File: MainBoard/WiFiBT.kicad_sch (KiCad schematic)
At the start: 8 parts, among them U2 ESP32-MINI-1-H4

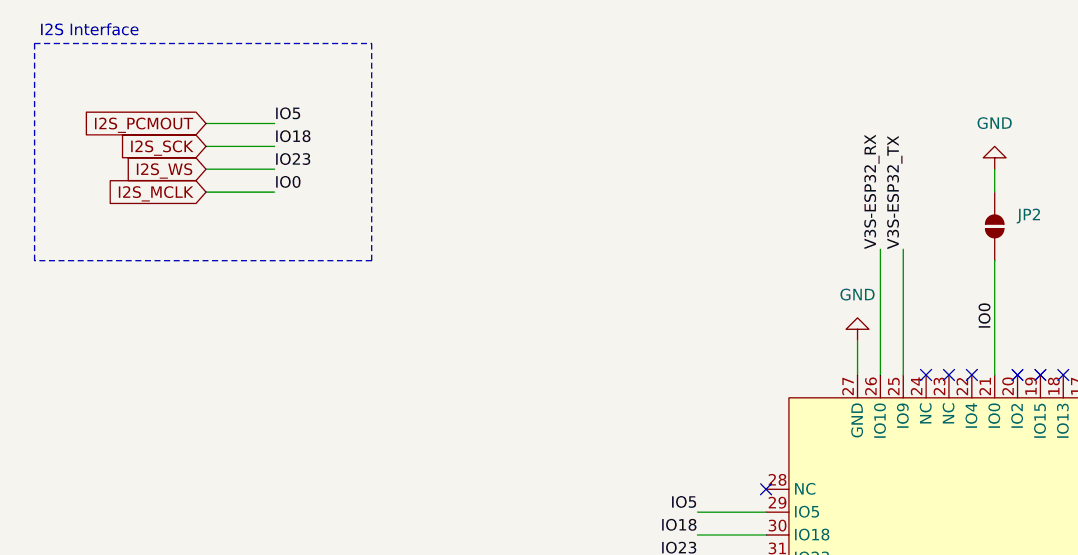
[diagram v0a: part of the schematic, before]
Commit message: footprints for wheel + power changes for v3s
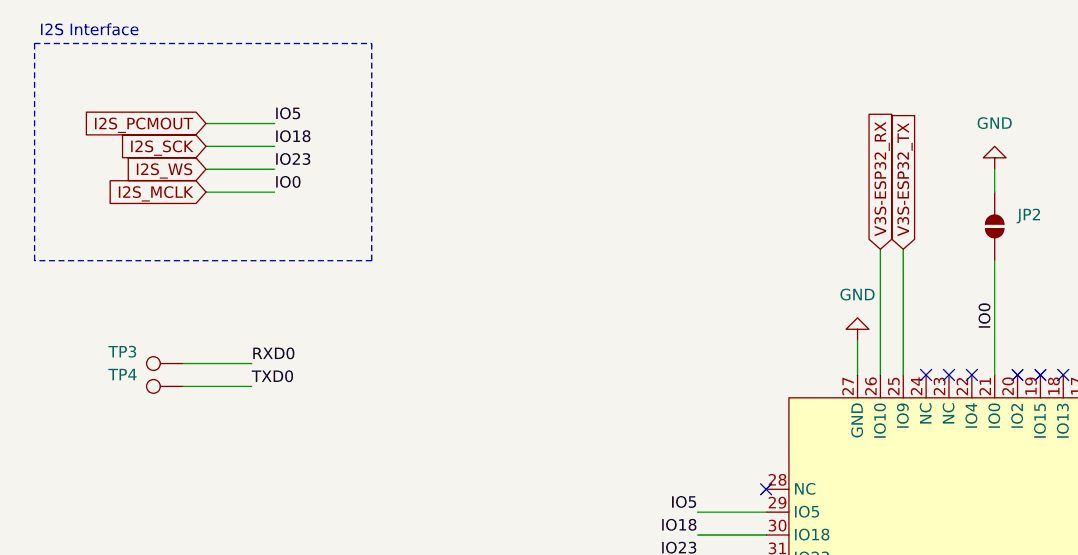
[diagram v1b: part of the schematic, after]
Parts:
- added TP3, TP4: TestPoint, symbol Connector:TestPoint
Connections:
- net RXD0: now also TP3.1
- net TXD0: now also TP4.1
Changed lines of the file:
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@@
+	(wire
+		(pts
+			(xy 44.45 62.23) (xy 36.83 62.23)
+		)
+		(stroke
+			(width 0)
+			(type default)
+		)
+	)
 	(wire
 		(pts
@@
 		(pts
 			(xy 111.76 59.69) (xy 111.76 63.5)
+		)
+		(stroke
+			(width 0)
+			(type default)
+		)
+	)
+	(wire
+		(pts
+			(xy 44.45 64.77) (xy 36.83 64.77)
 		)
 		(stroke
@@
 		)
 	)
+	(label "RXD0"
+		(at 44.45 62.23 0)
+		(effects
+			(font
+				(size 1.27 1.27)
+			)
+			(justify left bottom)
+		)
+	)
 	(label "IO23"
 		(at 46.99 40.64 0)
@@
 		)
 	)
+	(label "TXD0"
+		(at 44.45 64.77 0)
+		(effects
+			(font
+				(size 1.27 1.27)
+			)
+			(justify left bottom)
+		)
+	)
 	(label "IO23"
 		(at 93.98 83.82 180)
@@
 		)
 	)
-	(label "V3S-ESP32_RX"
-		(at 114.3 49.53 90)
-		(effects
-			(font
-				(size 1.27 1.27)
-			)
-			(justify left bottom)
-		)
-	)
 	(label "IO18"
 		(at 46.99 38.1 0)
@@
 		)
 	)
-	(label "V3S-ESP32_TX"
-		(at 116.84 49.53 90)
-		(effects
-			(font
-				(size 1.27 1.27)
-			)
-			(justify left bottom)
+	(global_label "V3S-ESP32_RX"
+		(shape input)
+		(at 114.3 49.53 90)
+		(fields_autoplaced yes)
+		(effects
+			(font
+				(size 1.27 1.27)
+			)
+			(justify left)
+		)
+		(property "Intersheetrefs" "${INTERSHEET_REFS}"
+			(at 114.3 31.9702 90)
+			(effects
+				(font
+					(size 1.27 1.27)
+				)
+				(justify left)
+				(hide yes)
+			)
 		)
 	)
@@
 				)
 				(justify right)
+				(hide yes)
+			)
+		)
+	)
+	(global_label "V3S-ESP32_TX"
+		(shape input)
+		(at 116.84 49.53 90)
+		(fields_autoplaced yes)
+		(effects
+			(font
+				(size 1.27 1.27)
+			)
+			(justify left)
+		)
+		(property "Intersheetrefs" "${INTERSHEET_REFS}"
+			(at 116.84 32.2726 90)
+			(effects
+				(font
+					(size 1.27 1.27)
+				)
+				(justify left)
 				(hide yes)
 			)
@@
 	)
 	(symbol
+		(lib_id "Connector:TestPoint")
+		(at 36.83 62.23 90)
+		(mirror x)
+		(unit 1)
+		(exclude_from_sim no)
+		(in_bom yes)
+		(on_board yes)
+		(dnp no)
+		(fields_autoplaced yes)
+		(property "Reference" "TP3"
+			(at 31.75 60.9599 90)
+			(effects
+				(font
+					(size 1.27 1.27)
+				)
+				(justify left)
+			)
+		)
+		(property "Value" "TestPoint"
+			(at 31.75 63.4999 90)
+			(effects
+				(font
+					(size 1.27 1.27)
+				)
+				(justify left)
+				(hide yes)
+			)
+		)
+		(property "Footprint" ""
+			(at 36.83 67.31 0)
+			(effects
+				(font
+					(size 1.27 1.27)
+				)
+				(hide yes)
+			)
+		)
+		(property "Datasheet" "~"
+			(at 36.83 67.31 0)
+			(effects
+				(font
+					(size 1.27 1.27)
+				)
+				(hide yes)
+			)
+		)
+		(property "Description" "test point"
+			(at 36.83 62.23 0)
+			(effects
+				(font
+					(size 1.27 1.27)
+				)
+				(hide yes)
+			)
+		)
+		(pin "1"
+		)
+		(instances
+			(project ""
+				(path "/8a2ca4d7-9471-417b-a346-3246fc9a2f27/afa0f51f-4585-49c6-821b-c9484c1d19a7"
+					(reference "TP3")
+					(unit 1)
+				)
+			)
+		)
+	)
+	(symbol
 		(lib_id "power:GND")
 		(at 111.76 59.69 180)
@@
 					(unit 1)
 				)
+			)
+		)
+	)
+	(symbol
+		(lib_id "Connector:TestPoint")
+		(at 36.83 64.77 90)
+		(mirror x)
+		(unit 1)
+		(exclude_from_sim no)
+		(in_bom yes)
+		(on_board yes)
+		(dnp no)
+		(fields_autoplaced yes)
+		(property "Reference" "TP4"
+			(at 31.75 63.4999 90)
+			(effects
+				(font
+					(size 1.27 1.27)
+				)
+				(justify left)
+			)
+		)
+		(property "Value" "TestPoint"
+			(at 31.75 66.0399 90)
+			(effects
+				(font
+					(size 1.27 1.27)
+				)
+				(justify left)
+				(hide yes)
+			)
+		)
+		(property "Footprint" ""
+			(at 36.83 69.85 0)
+			(effects
+				(font
+					(size 1.27 1.27)
+				)
+				(hide yes)
+			)
+		)
+		(property "Datasheet" "~"
+			(at 36.83 69.85 0)
+			(effects
+				(font
+					(size 1.27 1.27)
+				)
+				(hide yes)
+			)
+		)
+		(property "Description" "test point"
+			(at 36.83 64.77 0)
+			(effects
+				(font
+					(size 1.27 1.27)
+				)
+				(hide yes)
+			)
+		)
+		(pin "1"
+		)
+		(instances
+			(project "MainBoard"
+				(path "/8a2ca4d7-9471-417b-a346-3246fc9a2f27/afa0f51f-4585-49c6-821b-c9484c1d19a7"
+					(reference "TP4")
+					(unit 1)
+				)

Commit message: minor power changes
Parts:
- C30, C31, C32, C33: footprint (none) -> Capacitor_SMD:C_0402_1005Metric
- JP1, JP2: footprint (none) -> Jumper:SolderJumper-2_P1.3mm_Open_Pad1.0x1.5mm
- R25: footprint (none) -> Resistor_SMD:R_0402_1005Metric
- TP3, TP4: footprint (none) -> TestPoint:TestPoint_Pad_1.5x1.5mm
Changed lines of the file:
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@@
 			)
 		)
-		(property "Footprint" ""
+		(property "Footprint" "Jumper:SolderJumper-2_P1.3mm_Open_Pad1.0x1.5mm"
 			(at 246.38 38.1 0)
 			(effects
@@
 			)
 		)
-		(property "Footprint" ""
+		(property "Footprint" "Resistor_SMD:R_0402_1005Metric"
 			(at 179.832 78.74 90)
 			(effects
@@
 			)
 		)
-		(property "Footprint" ""
+		(property "Footprint" "Capacitor_SMD:C_0402_1005Metric"
 			(at 250.19 43.4848 0)
 			(effects
@@
 			)
 		)
-		(property "Footprint" ""
+		(property "Footprint" "Capacitor_SMD:C_0402_1005Metric"
 			(at 182.5752 118.11 0)
 			(effects
@@
 			)
 		)
-		(property "Footprint" ""
+		(property "Footprint" "Jumper:SolderJumper-2_P1.3mm_Open_Pad1.0x1.5mm"
 			(at 127 46.99 0)
 			(effects
@@
 			)
 		)
-		(property "Footprint" ""
+		(property "Footprint" "Capacitor_SMD:C_0402_1005Metric"
 			(at 197.8152 118.11 0)
 			(effects
@@
 			)
 		)
-		(property "Footprint" ""
+		(property "Footprint" "Capacitor_SMD:C_0402_1005Metric"
 			(at 190.1952 118.11 0)
 			(effects
@@
 			)
 		)
-		(property "Footprint" ""
+		(property "Footprint" "TestPoint:TestPoint_Pad_1.5x1.5mm"
 			(at 36.83 67.31 0)
 			(effects
@@
 			)
 		)
-		(property "Footprint" ""
+		(property "Footprint" "TestPoint:TestPoint_Pad_1.5x1.5mm"
 			(at 36.83 69.85 0)
 			(effects

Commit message: layout and starting routing
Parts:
- added SW1, SW2, SW3, SW4, SW5: TS3735A 250GF 030, easyeda2kicad:SW-SMD_4P-L3.7-W3.7-P2.70-LS3.7, symbol easyeda2kicad:TS3735A250GF030
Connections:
- net GND: now also SW1.1, SW1.2, SW2.1, SW2.2, SW3.1, SW3.2, SW4.1, SW4.2, SW5.1, SW5.2
- net IO35: now reaches U2.10 (I35)
- net IO35: now also SW4.3, SW4.4
- net IO32: now reaches U2.11 (IO32)
- net IO32: now also SW3.3, SW3.4
- net IO33: now reaches U2.12 (IO33)
- net IO33: now also SW2.3, SW2.4
- net IO25: now reaches U2.13 (IO25)
- net IO25: now also SW1.3, SW1.4
- net IO34: now reaches U2.9 (I34)
- net IO34: now also SW5.3, SW5.4
- no-connect marks 24 -> 19
